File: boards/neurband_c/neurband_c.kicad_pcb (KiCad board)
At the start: 4 copper layers, 28.7 x 27 mm, 67 parts, among them J1 FPC 20p 0.5mm (electrode flex), J2 LiPo 3.7V (protected), J3 Charge 5V (magnetic pads), SW1 WAKE / MARK, U1 nRF52832-QFAA, U2 ADS1298IPAGR, U3 XC6206P332MR, U4 TP4054, U5 LSM6DSL, Y1 32MHz 8pF

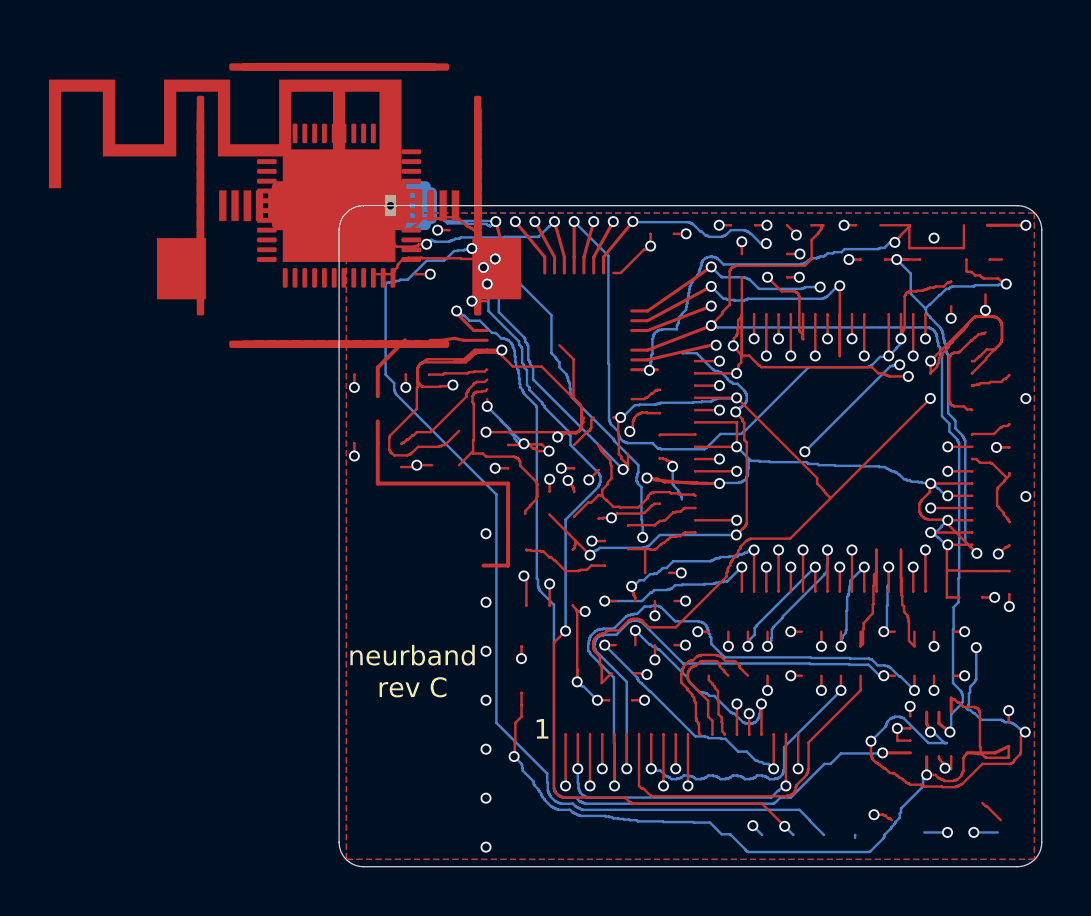
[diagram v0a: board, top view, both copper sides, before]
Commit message: Rev C pre-order rework: analog/RF/DFM fixes, assembly guide and animation
Main board (re-laid out by the layout owner after independent pre-order reviews):
- digital lines (I2C, IMU_INT) moved out of the electrode input field; worst
  coupling 0.89 fF, injected noise <= 0.057 uVrms, P/N mismatch <= 0.71 pF
- local regulator output loop, local ADS/nRF bypassing, C33 at AVDD1, 0603 bulk caps
- RLDIN behind the 100k bias resistor, 10k input arrays (ESD), 12 pF bias RF shunt
- nine tented GND vias in the nRF exposed pad, stitching <= 3 mm in RF/AFE
- footprints carry the fab's 0 deg so the raw position file is correct;
  pin-1/cathode silkscreen, thermal reliefs, 0.5 mm edge pour setback
- DRC 0 / unconnected 0 / parity 0; BOM consolidated to 25 part types

Electrode flex: coverlay closed at the alignment holes, filled stiffener region,
ordering notes; marked not orderable through the rigid-board flow.

Reviews and simulations: analog/noise, on-wrist antenna FDTD (keep the printed
IFA), manufacturing and CPL check against the fab's own footprints.

Mechanics and docs: lead gate, J1 access, snap tolerances; step-by-step build
guide with images and an assembly animation; honest cost update.

Co-Authored-By: Claude Opus 5.5 <noreply@anthropic.com>
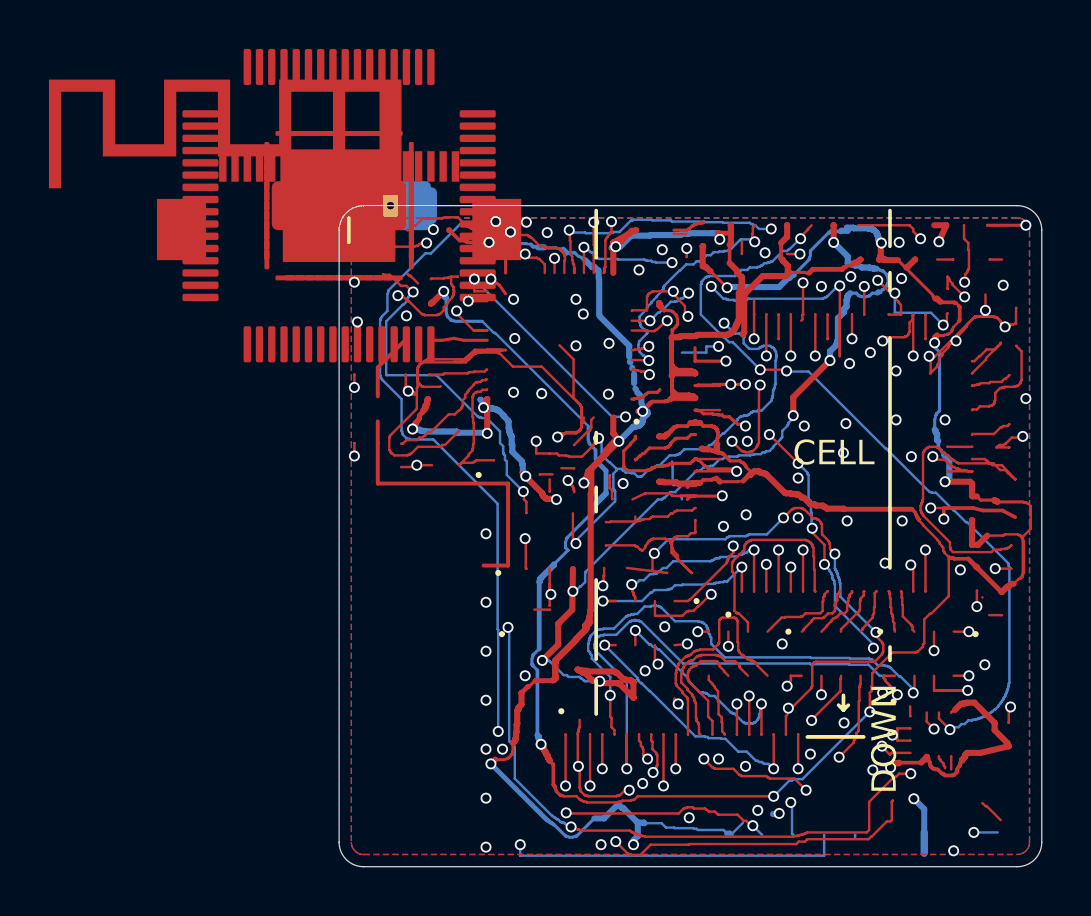
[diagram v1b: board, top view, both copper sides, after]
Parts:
- added C33: 1uF, Capacitor_SMD:C_0402_1005Metric, F.Cu at (0.00, 0.00)
- added C34: 12pF, Capacitor_SMD:C_0402_1005Metric, F.Cu at (0.00, 0.00)
- C16, C25: value 4.7uF -> 10uF
- C28, C6: footprint Capacitor_SMD:C_0402_1005Metric -> Capacitor_SMD:C_0603_1608Metric
- J1: footprint neurband:XUNPU_FPC-05F-20PH20 -> neurband:XUNPU_FPC-05F-20PH20_Centroid
- R10, R9: value 4.7k -> 10k
- RN1, RN2, RN3, RN4: value 4.7k -> 10k; footprint Resistor_SMD:R_Array_Convex_4x0603 -> neurband:R_Array_Convex_4x0603_FabZero
- U1: footprint Package_DFN_QFN:QFN-48-1EP_6x6mm_P0.4mm_EP4.6x4.6mm -> neurband:QFN-48-1EP_6x6mm_P0.4mm_EP4.6x4.6mm_FabZero
- U2: footprint Package_QFP:TQFP-64_10x10mm_P0.5mm -> neurband:TQFP-64_10x10mm_P0.5mm_FabZero
- U3: footprint Package_TO_SOT_SMD:SOT-23-3 -> neurband:SOT-23-3_FabZero
- U4: footprint Package_TO_SOT_SMD:SOT-23-5 -> neurband:SOT-23-5_FabZero
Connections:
- C12 pad 1: Net-(U2-RLDOUT) -> /RLD_DRV
- R1 pad 1: Net-(U2-RLDOUT) -> /RLD_DRV
- R2 pad 1: Net-(U2-RLDOUT) -> /RLD_DRV
- U2 pad 62: /BIAS_E -> /RLD_DRV
- U2 pad 63: Net-(U2-RLDOUT) -> /RLD_DRV
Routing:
- net +3V3A: track 65.4 -> 108.4 mm, vias 12 -> 8
- net /RLDREF: track 8.36 -> 35.3 mm, vias 0 -> 2
- net VBAT: track 85.4 -> 59.5 mm, vias 9 -> 7
- net +3V3: track 163.4 -> 144.4 mm, vias 19 -> 16
- net GND: track 97.8 -> 115.0 mm, vias 63 -> 103
- net /BIAS_E: track 28.5 -> 43.6 mm, vias 4 -> 8
- net /I2C_SDA: track 53.2 -> 40.0 mm, vias 6 -> 3
- net Net-(U4-PROG): track 3.68 -> 15.0 mm, vias 0 -> 2
- net /ADC_PWDN: track 32.2 -> 22.3 mm, vias 3 -> 5
- net Net-(U2-VREFP): track 4.19 -> 13.8 mm
- net VCHG: track 18.8 -> 27.1 mm, vias 3 -> 5
- net /RLD_DRV: track 0.00 -> 8.04 mm
- net /IMU_INT: track 39.1 -> 44.8 mm, vias 2 -> 5
- net /E1N: track 25.7 -> 31.2 mm
- net /ADC_START: track 25.7 -> 20.5 mm, vias 2 -> 3
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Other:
- board text added: "CELL"
- board text added: "DOWN"
- board text removed: "1"
- board text removed: "neurband"
- board text removed: "neurband / C"
